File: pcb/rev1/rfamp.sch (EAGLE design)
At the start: 20 parts, among them IC1 NCP700BSN-30, IC2 ADL5523, X1 SAW-B3721

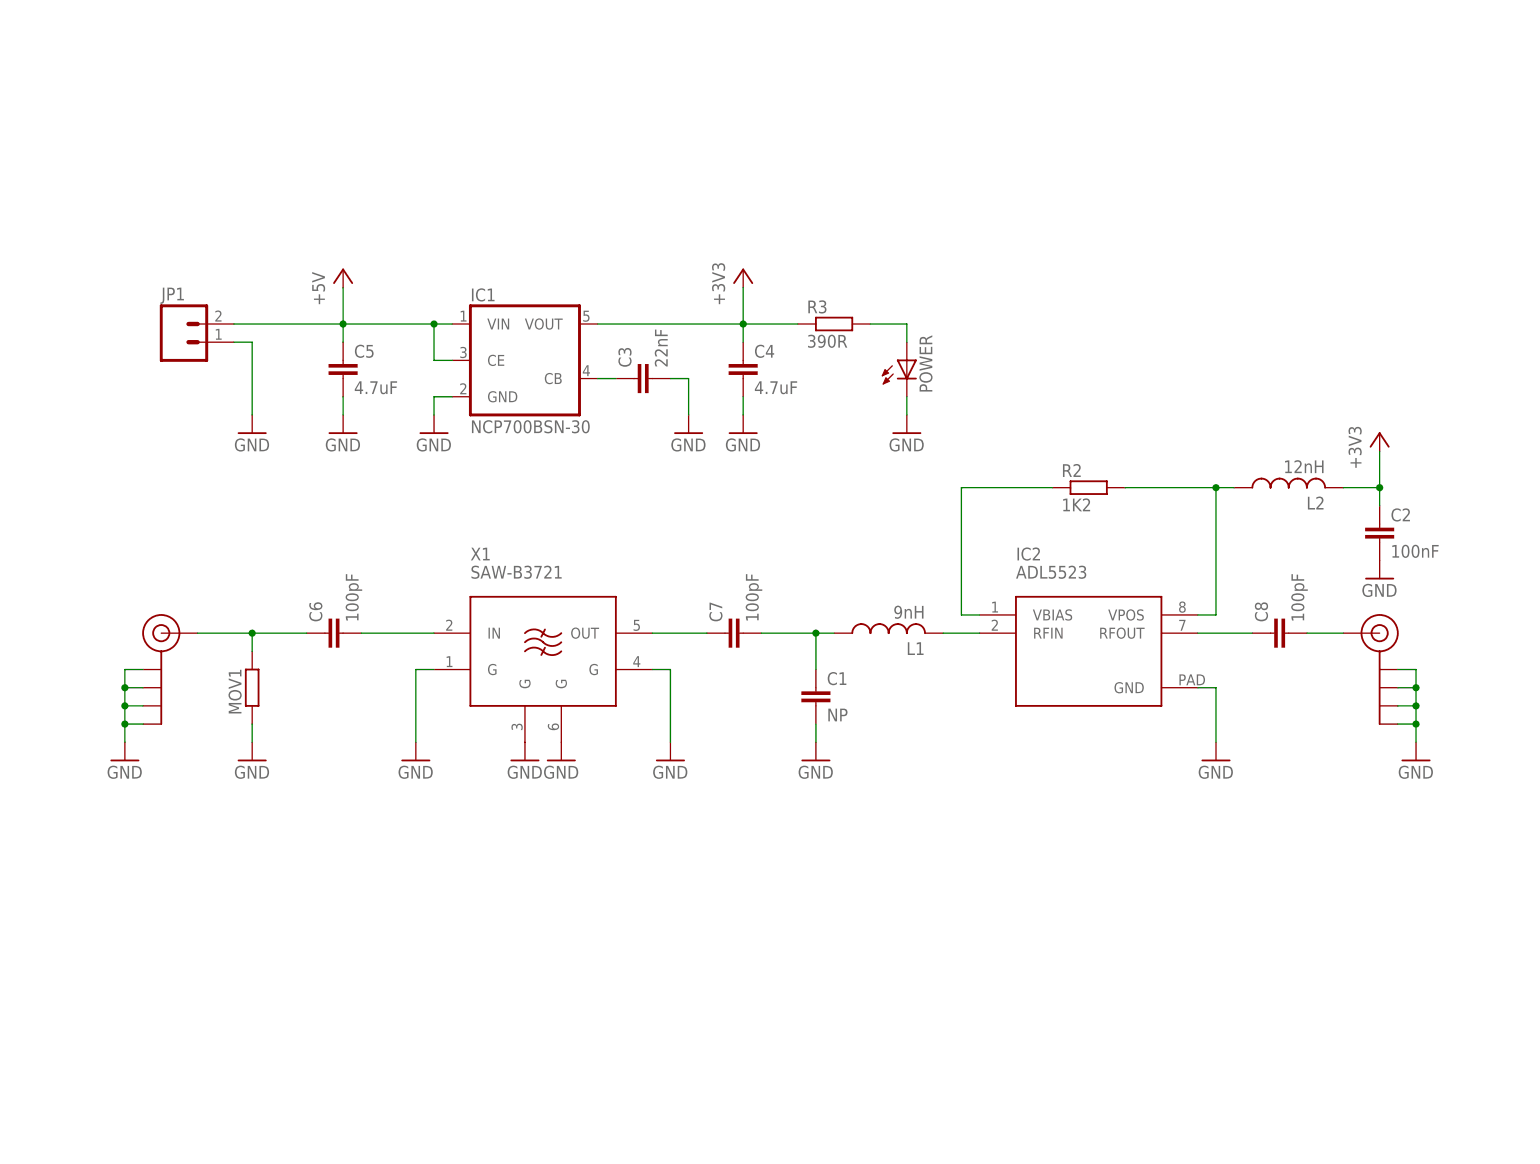
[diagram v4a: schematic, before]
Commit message: Add schematic annotation.
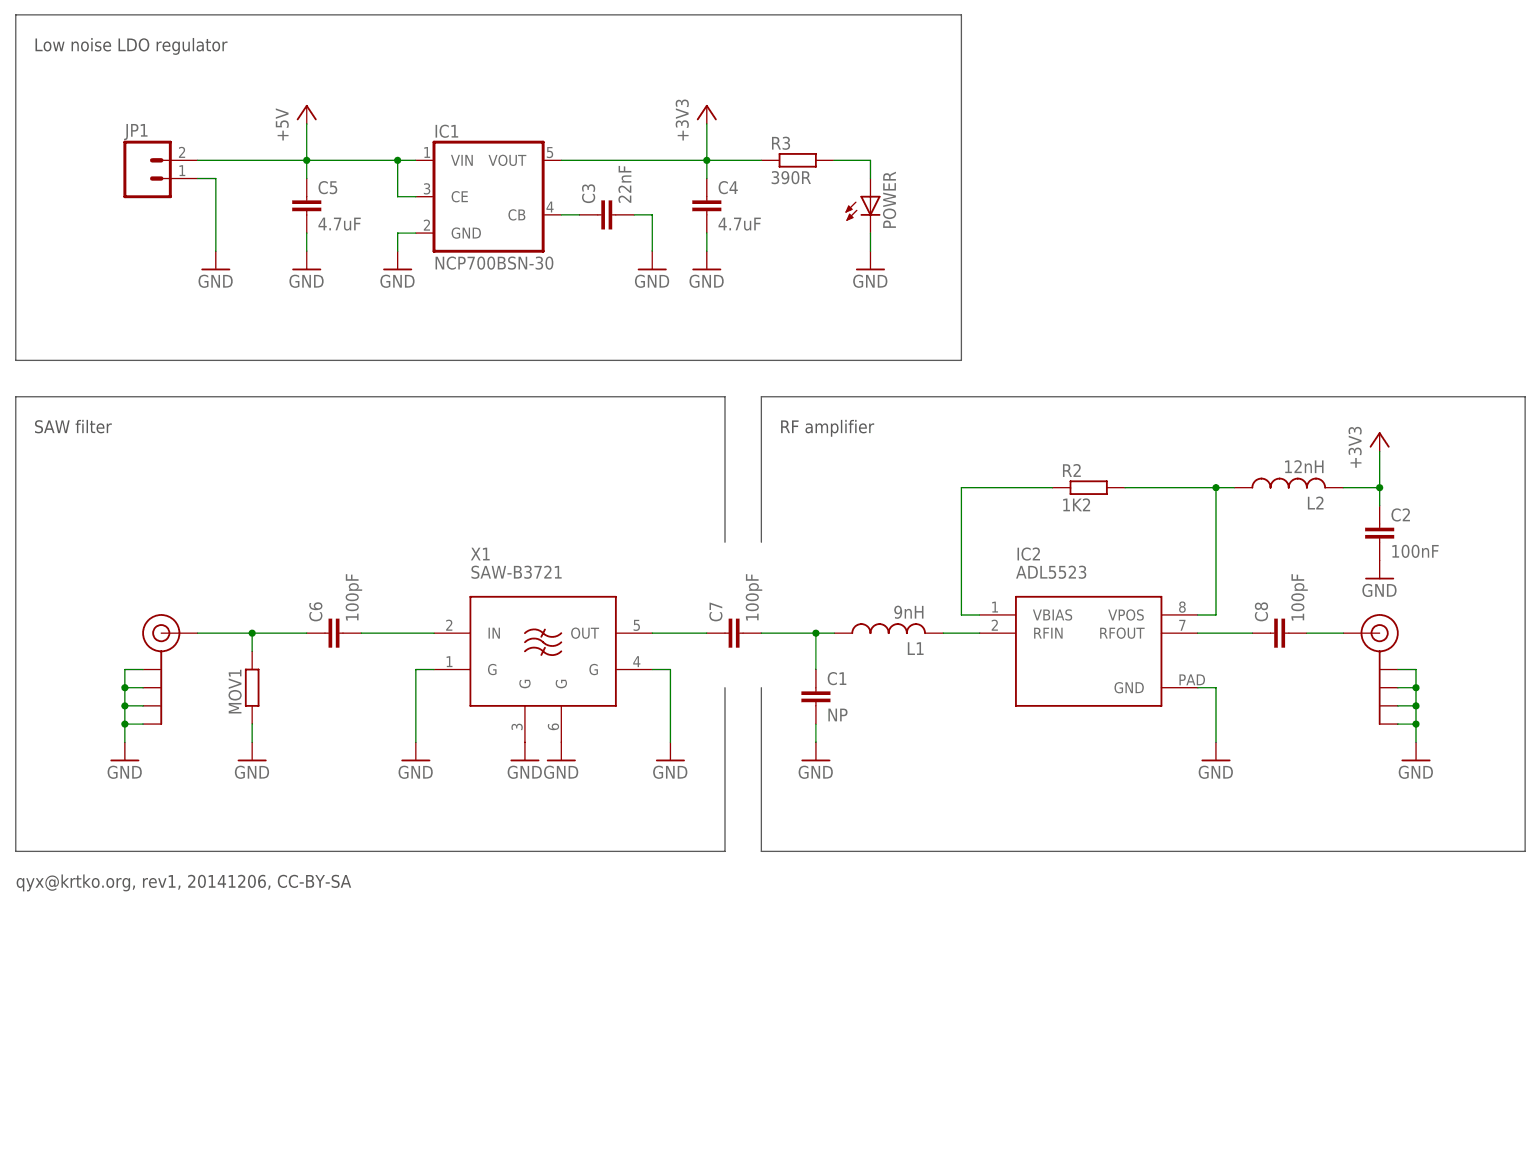
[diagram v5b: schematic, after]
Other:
- note added: "Low noise LDO regulator"
- note added: "RF amplifier"
- note added: "SAW filter"
- note added: "qyx@krtko.org, rev1, 20141206, CC-BY-SA"
- moved on the sheet: C3, C4, C5, IC1, JP1, POWER, R3
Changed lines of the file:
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@@
 <sheet>
 <plain>
+<wire x1="-22.86" y1="157.48" x2="109.22" y2="157.48" width="0.1524" layer="97"/>
+<wire x1="109.22" y1="157.48" x2="109.22" y2="109.22" width="0.1524" layer="97"/>
+<wire x1="109.22" y1="109.22" x2="-22.86" y2="109.22" width="0.1524" layer="97"/>
+<wire x1="-22.86" y1="109.22" x2="-22.86" y2="157.48" width="0.1524" layer="97"/>
+<wire x1="-22.86" y1="104.14" x2="76.2" y2="104.14" width="0.1524" layer="97"/>
+<wire x1="76.2" y1="104.14" x2="76.2" y2="83.82" width="0.1524" layer="97"/>
+<wire x1="76.2" y1="63.5" x2="76.2" y2="40.64" width="0.1524" layer="97"/>
+<wire x1="76.2" y1="40.64" x2="-22.86" y2="40.64" width="0.1524" layer="97"/>
+<wire x1="-22.86" y1="40.64" x2="-22.86" y2="104.14" width="0.1524" layer="97"/>
+<wire x1="81.28" y1="63.5" x2="81.28" y2="40.64" width="0.1524" layer="97"/>
+<wire x1="81.28" y1="40.64" x2="187.96" y2="40.64" width="0.1524" layer="97"/>
+<wire x1="187.96" y1="40.64" x2="187.96" y2="104.14" width="0.1524" layer="97"/>
+<wire x1="187.96" y1="104.14" x2="81.28" y2="104.14" width="0.1524" layer="97"/>
+<wire x1="81.28" y1="104.14" x2="81.28" y2="83.82" width="0.1524" layer="97"/>
+<text x="-22.86" y="35.56" size="1.778" layer="97">qyx@krtko.org, rev1, 20141206, CC-BY-SA</text>
+<text x="-20.32" y="99.06" size="1.778" layer="97">SAW filter</text>
+<text x="83.82" y="99.06" size="1.778" layer="97">RF amplifier</text>
+<text x="-20.32" y="152.4" size="1.778" layer="97">Low noise LDO regulator</text>
 </plain>
 <instances>
 <instance part="GND1" gate="1" x="-7.62" y="53.34"/>
-<instance part="GND2" gate="1" x="22.86" y="99.06"/>
+<instance part="GND2" gate="1" x="17.78" y="121.92"/>
 <instance part="GND3" gate="1" x="172.72" y="53.34"/>
 <instance part="X1" gate="G$1" x="53.34" y="66.04"/>
@@
 <instance part="GND10" gate="1" x="167.64" y="78.74"/>
 <instance part="+3V1" gate="G$1" x="167.64" y="99.06"/>
-<instance part="+3V2" gate="G$1" x="78.74" y="121.92"/>
-<instance part="IC1" gate="G$1" x="48.26" y="109.22"/>
-<instance part="C3" gate="G$1" x="63.5" y="106.68" rot="R90"/>
-<instance part="C4" gate="G$1" x="78.74" y="109.22"/>
-<instance part="C5" gate="G$1" x="22.86" y="109.22"/>
-<instance part="GND11" gate="1" x="35.56" y="99.06"/>
-<instance part="GND12" gate="1" x="71.12" y="99.06"/>
-<instance part="GND13" gate="1" x="78.74" y="99.06"/>
-<instance part="P+1" gate="1" x="22.86" y="121.92"/>
-<instance part="JP1" gate="G$1" x="0" y="111.76"/>
-<instance part="GND14" gate="1" x="10.16" y="99.06"/>
+<instance part="+3V2" gate="G$1" x="73.66" y="144.78"/>
+<instance part="IC1" gate="G$1" x="43.18" y="132.08"/>
+<instance part="C3" gate="G$1" x="58.42" y="129.54" rot="R90"/>
+<instance part="C4" gate="G$1" x="73.66" y="132.08"/>
+<instance part="C5" gate="G$1" x="17.78" y="132.08"/>
+<instance part="GND11" gate="1" x="30.48" y="121.92"/>
+<instance part="GND12" gate="1" x="66.04" y="121.92"/>
+<instance part="GND13" gate="1" x="73.66" y="121.92"/>
+<instance part="P+1" gate="1" x="17.78" y="144.78"/>
+<instance part="JP1" gate="G$1" x="-5.08" y="134.62"/>
+<instance part="GND14" gate="1" x="5.08" y="121.92"/>
 <instance part="IC2" gate="G$1" x="127" y="68.58"/>
 <instance part="GND15" gate="1" x="144.78" y="53.34"/>
-<instance part="R3" gate="G$1" x="91.44" y="114.3"/>
-<instance part="POWER" gate="G$1" x="101.6" y="109.22"/>
-<instance part="GND16" gate="1" x="101.6" y="99.06"/>
+<instance part="R3" gate="G$1" x="86.36" y="137.16"/>
+<instance part="POWER" gate="G$1" x="96.52" y="132.08"/>
+<instance part="GND16" gate="1" x="96.52" y="121.92"/>
 <instance part="J$1" gate="1" x="-2.54" y="71.12"/>
 <instance part="J$2" gate="1" x="167.64" y="71.12" rot="MR0"/>
@@
 <pinref part="C5" gate="G$1" pin="2"/>
 <pinref part="GND2" gate="1" pin="GND"/>
-<wire x1="22.86" y1="104.14" x2="22.86" y2="101.6" width="0.1524" layer="91"/>
+<wire x1="17.78" y1="127" x2="17.78" y2="124.46" width="0.1524" layer="91"/>
 </segment>
 <segment>
 <pinref part="IC1" gate="G$1" pin="GND"/>
 <pinref part="GND11" gate="1" pin="GND"/>
-<wire x1="38.1" y1="104.14" x2="35.56" y2="104.14" width="0.1524" layer="91"/>
-<wire x1="35.56" y1="104.14" x2="35.56" y2="101.6" width="0.1524" layer="91"/>
+<wire x1="33.02" y1="127" x2="30.48" y2="127" width="0.1524" layer="91"/>
+<wire x1="30.48" y1="127" x2="30.48" y2="124.46" width="0.1524" layer="91"/>
 </segment>
 <segment>
 <pinref part="C4" gate="G$1" pin="2"/>
 <pinref part="GND13" gate="1" pin="GND"/>
-<wire x1="78.74" y1="104.14" x2="78.74" y2="101.6" width="0.1524" layer="91"/>
+<wire x1="73.66" y1="127" x2="73.66" y2="124.46" width="0.1524" layer="91"/>
 </segment>
 <segment>
 <pinref part="C3" gate="G$1" pin="2"/>
 <pinref part="GND12" gate="1" pin="GND"/>
-<wire x1="68.58" y1="106.68" x2="71.12" y2="106.68" width="0.1524" layer="91"/>
-<wire x1="71.12" y1="106.68" x2="71.12" y2="101.6" width="0.1524" layer="91"/>
+<wire x1="63.5" y1="129.54" x2="66.04" y2="129.54" width="0.1524" layer="91"/>
+<wire x1="66.04" y1="129.54" x2="66.04" y2="124.46" width="0.1524" layer="91"/>
 </segment>
 <segment>
 <pinref part="JP1" gate="G$1" pin="1"/>
 <pinref part="GND14" gate="1" pin="GND"/>
-<wire x1="7.62" y1="111.76" x2="10.16" y2="111.76" width="0.1524" layer="91"/>
-<wire x1="10.16" y1="111.76" x2="10.16" y2="101.6" width="0.1524" layer="91"/>
+<wire x1="2.54" y1="134.62" x2="5.08" y2="134.62" width="0.1524" layer="91"/>
+<wire x1="5.08" y1="134.62" x2="5.08" y2="124.46" width="0.1524" layer="91"/>
 </segment>
 <segment>
@@
 <pinref part="POWER" gate="G$1" pin="C"/>
 <pinref part="GND16" gate="1" pin="GND"/>
-<wire x1="101.6" y1="104.14" x2="101.6" y2="101.6" width="0.1524" layer="91"/>
+<wire x1="96.52" y1="127" x2="96.52" y2="124.46" width="0.1524" layer="91"/>
 </segment>
 <segment>
@@
 <pinref part="IC1" gate="G$1" pin="VOUT"/>
 <pinref part="C4" gate="G$1" pin="1"/>
-<wire x1="58.42" y1="114.3" x2="78.74" y2="114.3" width="0.1524" layer="91"/>
-<wire x1="78.74" y1="114.3" x2="78.74" y2="111.76" width="0.1524" layer="91"/>
+<wire x1="53.34" y1="137.16" x2="73.66" y2="137.16" width="0.1524" layer="91"/>
+<wire x1="73.66" y1="137.16" x2="73.66" y2="134.62" width="0.1524" layer="91"/>
 <pinref part="+3V2" gate="G$1" pin="+3V3"/>
-<wire x1="78.74" y1="114.3" x2="78.74" y2="119.38" width="0.1524" layer="91"/>
-<junction x="78.74" y="114.3"/>
+<wire x1="73.66" y1="137.16" x2="73.66" y2="142.24" width="0.1524" layer="91"/>
+<junction x="73.66" y="137.16"/>
 <pinref part="R3" gate="G$1" pin="1"/>
-<wire x1="78.74" y1="114.3" x2="86.36" y2="114.3" width="0.1524" layer="91"/>
+<wire x1="73.66" y1="137.16" x2="81.28" y2="137.16" width="0.1524" layer="91"/>
 </segment>
 </net>
@@
 <pinref part="C5" gate="G$1" pin="1"/>
 <pinref part="P+1" gate="1" pin="+5V"/>
-<wire x1="22.86" y1="111.76" x2="22.86" y2="114.3" width="0.1524" layer="91"/>
+<wire x1="17.78" y1="134.62" x2="17.78" y2="137.16" width="0.1524" layer="91"/>
 <pinref part="IC1" gate="G$1" pin="VIN"/>
-<wire x1="22.86" y1="114.3" x2="22.86" y2="119.38" width="0.1524" layer="91"/>
-<wire x1="38.1" y1="114.3" x2="35.56" y2="114.3" width="0.1524" layer="91"/>
-<junction x="22.86" y="114.3"/>
+<wire x1="17.78" y1="137.16" x2="17.78" y2="142.24" width="0.1524" layer="91"/>
+<wire x1="33.02" y1="137.16" x2="30.48" y2="137.16" width="0.1524" layer="91"/>
+<junction x="17.78" y="137.16"/>
 <pinref part="IC1" gate="G$1" pin="CE"/>
-<wire x1="35.56" y1="114.3" x2="22.86" y2="114.3" width="0.1524" layer="91"/>
-<wire x1="38.1" y1="109.22" x2="35.56" y2="109.22" width="0.1524" layer="91"/>
-<wire x1="35.56" y1="109.22" x2="35.56" y2="114.3" width="0.1524" layer="91"/>
-<junction x="35.56" y="114.3"/>
+<wire x1="30.48" y1="137.16" x2="17.78" y2="137.16" width="0.1524" layer="91"/>
+<wire x1="33.02" y1="132.08" x2="30.48" y2="132.08" width="0.1524" layer="91"/>
+<wire x1="30.48" y1="132.08" x2="30.48" y2="137.16" width="0.1524" layer="91"/>
+<junction x="30.48" y="137.16"/>
 <pinref part="JP1" gate="G$1" pin="2"/>
-<wire x1="7.62" y1="114.3" x2="22.86" y2="114.3" width="0.1524" layer="91"/>
+<wire x1="2.54" y1="137.16" x2="17.78" y2="137.16" width="0.1524" layer="91"/>
 </segment>
 </net>
@@
 <pinref part="C3" gate="G$1" pin="1"/>
 <pinref part="IC1" gate="G$1" pin="CB"/>
-<wire x1="60.96" y1="106.68" x2="58.42" y2="106.68" width="0.1524" layer="91"/>
+<wire x1="55.88" y1="129.54" x2="53.34" y2="129.54" width="0.1524" layer="91"/>
 </segment>
 </net>
@@
 <pinref part="R3" gate="G$1" pin="2"/>
 <pinref part="POWER" gate="G$1" pin="A"/>
-<wire x1="96.52" y1="114.3" x2="101.6" y2="114.3" width="0.1524" layer="91"/>
-<wire x1="101.6" y1="114.3" x2="101.6" y2="111.76" width="0.1524" layer="91"/>
-</segment>
-</net>
+<wire x1="91.44" y1="137.16" x2="96.52" y2="137.16" width="0.1524" layer="91"/>
+<wire x1="96.52" y1="137.16" x2="96.52" y2="134.62" width="0.1524" layer="91"/>
+</segment>
+</net>
